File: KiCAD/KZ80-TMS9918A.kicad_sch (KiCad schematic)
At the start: 39 parts

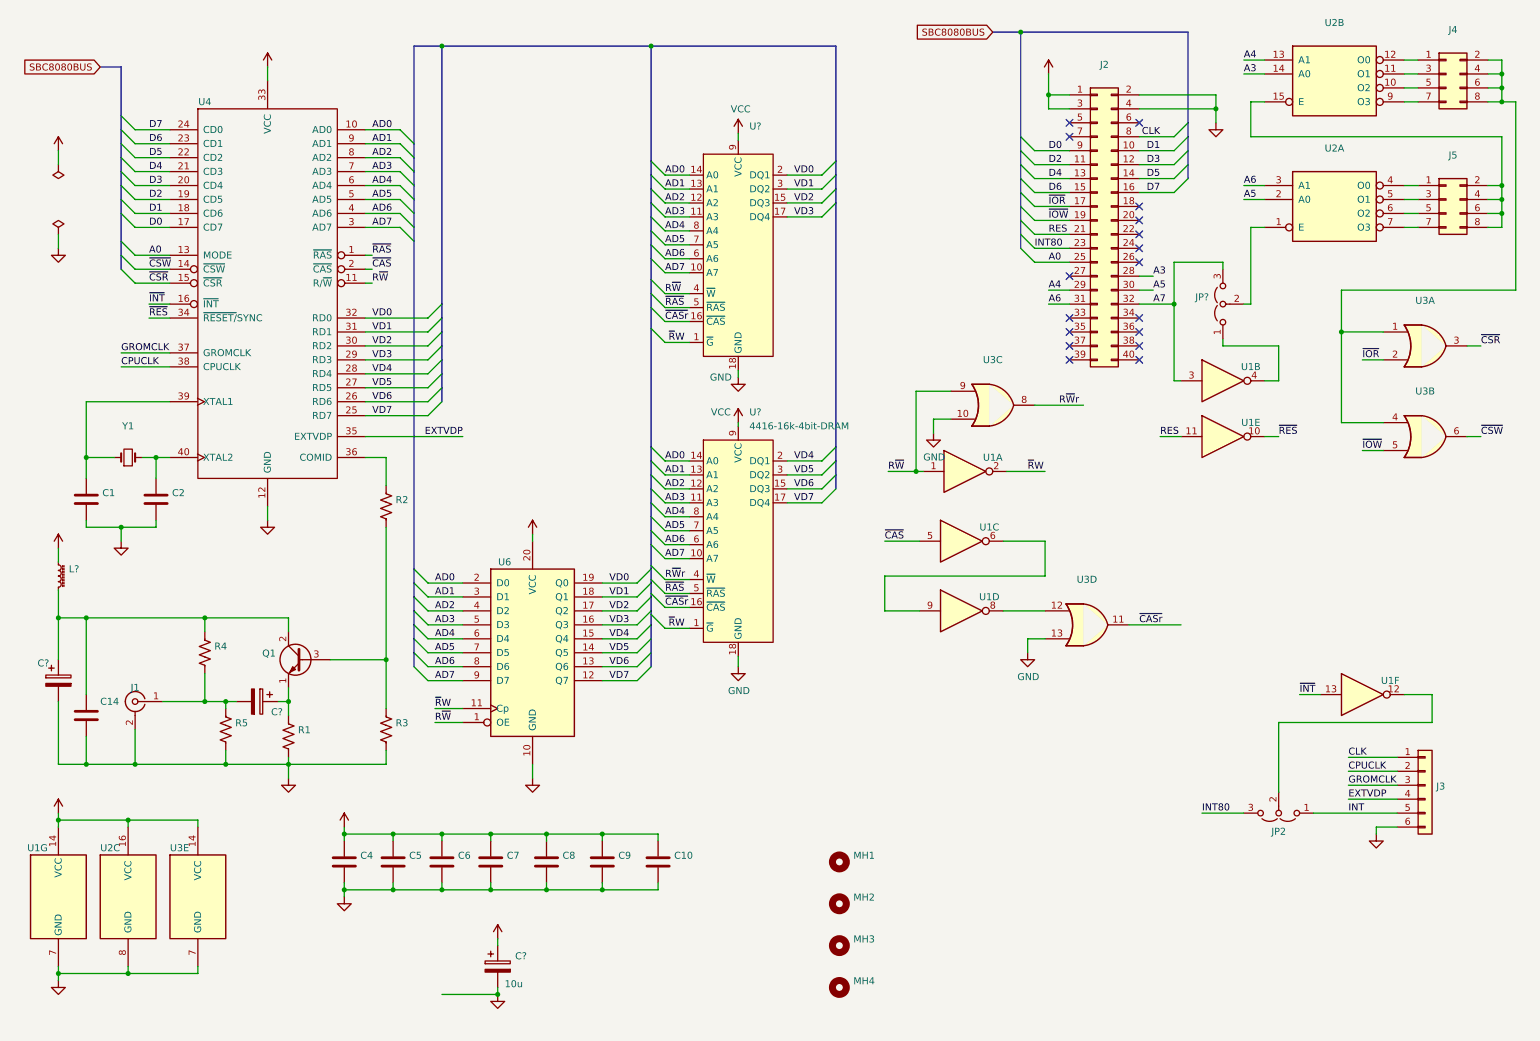
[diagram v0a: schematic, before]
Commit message: 4464 DRAM対応
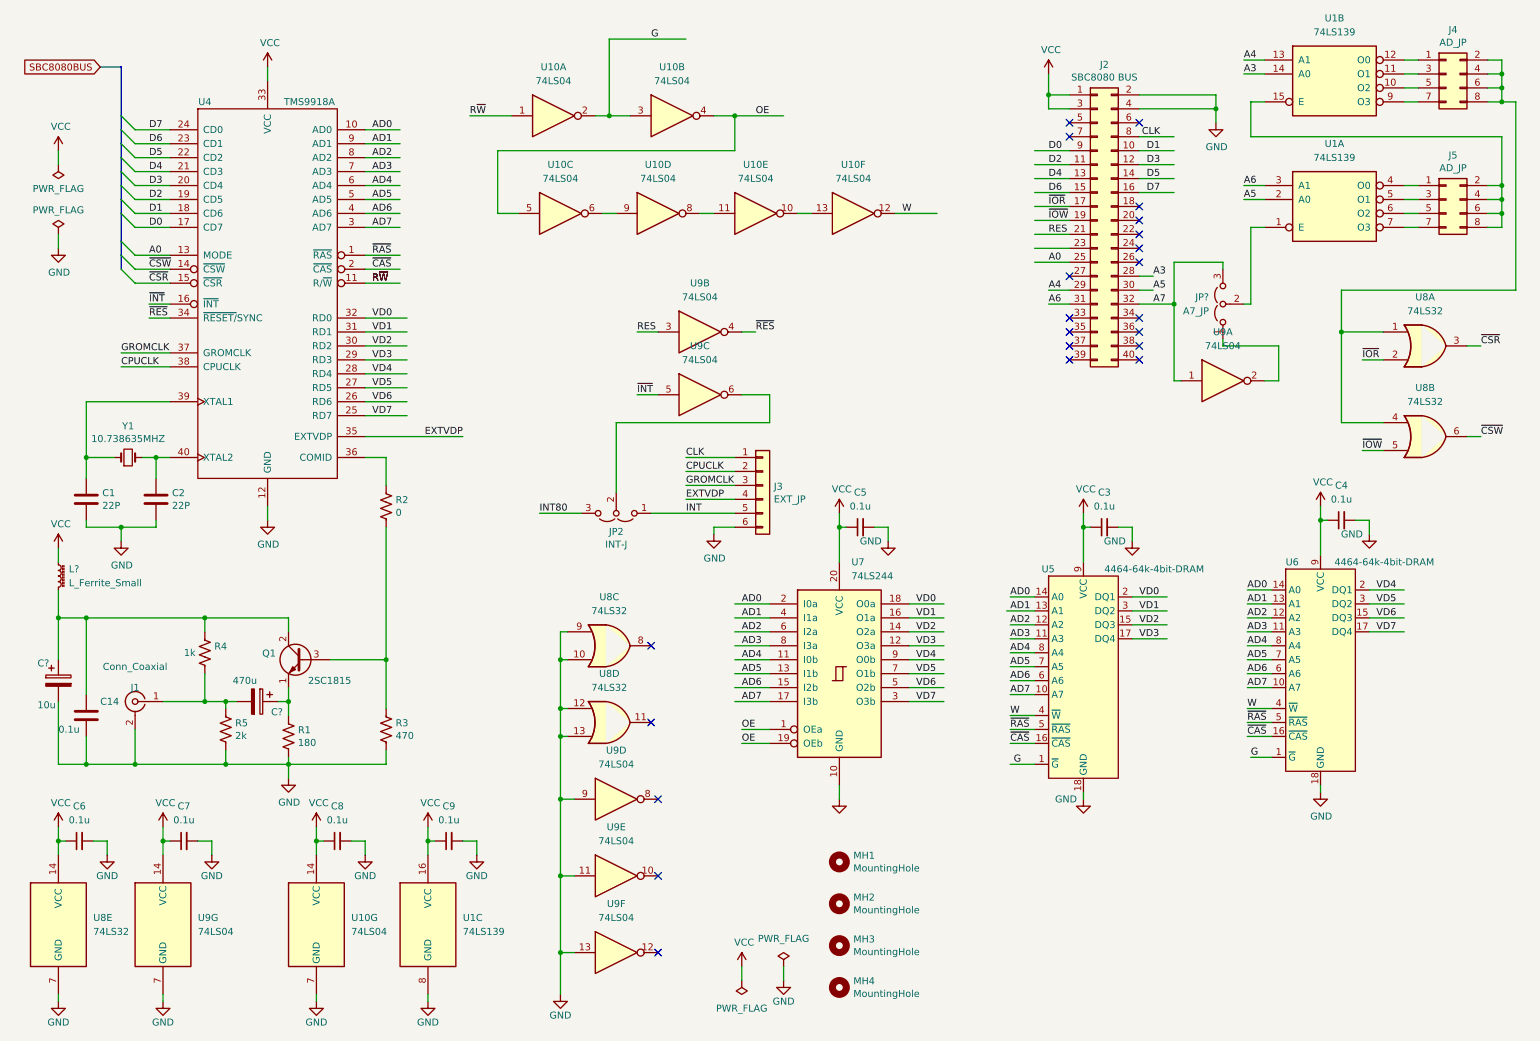
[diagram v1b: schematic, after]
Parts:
- removed C10, C4, C5, C6, C7, C8, C9: (no value), symbol Device:C
- removed C?: 10u, symbol Device:C_Polarized
- removed U1: (no value), symbol 74xx:74HCT04
- removed U2: (no value), symbol 74xx:74LS139
- removed U3: (no value), symbol 74xx:74LS32
- removed U6: (no value), symbol 74xx:74LS574
- removed U?: 4416-16k-4bit-DRAM, symbol DRAM:4416-16k-4bit-DRAM
- removed U?: (no value), symbol DRAM:4416-16k-4bit-DRAM
- added C3, C4, C5, C6, C7, C8, C9: 0.1u, symbol Device:C_Small
- added U1: 74LS139, symbol 74xx:74LS139
- added U10, U9: 74LS04, symbol 74xx:74LS04
- added U5, U6: 4464-64k-4bit-DRAM, symbol DRAM:4416-16k-4bit-DRAM
- added U7: 74LS244, symbol 74xx:74LS244
- added U8: 74LS32, symbol 74xx:74LS32
- C1, C2: value (none) -> 22P; footprint (none) -> Capacitor_THT:C_Disc_D3.0mm_W1.6mm_P2.50mm
- C14: value (none) -> 0.1u; footprint (none) -> Capacitor_THT:C_Disc_D3.0mm_W1.6mm_P2.50mm
- C?: value (none) -> 470u
- C?: value (none) -> 10u
- J1: value (none) -> Conn_Coaxial; footprint (none) -> RCACon:RCAConAE
- J2: value (none) -> SBC8080 BUS; footprint (none) -> Connector_PinHeader_2.54mm:PinHeader_2x20_P2.54mm_Horizontal
- J3: value (none) -> EXT_JP; footprint (none) -> Connector_PinHeader_2.54mm:PinHeader_1x06_P2.54mm_Horizontal
- J4, J5: value (none) -> AD_JP; footprint (none) -> Connector_PinHeader_2.54mm:PinHeader_2x04_P2.54mm_Vertical
- JP2: value (none) -> INT-J; footprint (none) -> Connector_PinHeader_2.54mm:PinHeader_1x03_P2.54mm_Vertical
- JP?: value (none) -> A7_JP
- L?: value (none) -> L_Ferrite_Small
- MH1, MH2, MH3, MH4: value (none) -> MountingHole; footprint (none) -> MountingHole:MountingHole_3.2mm_M3
- Q1: value (none) -> 2SC1815; footprint (none) -> Package_TO_SOT_THT:TO-92_Inline_Wide
- R1: value (none) -> 180; footprint (none) -> Resistor_THT:R_Axial_DIN0207_L6.3mm_D2.5mm_P10.16mm_Horizontal
- R2: value (none) -> 0; footprint (none) -> Resistor_THT:R_Axial_DIN0207_L6.3mm_D2.5mm_P10.16mm_Horizontal
- R3: value (none) -> 470; footprint (none) -> Resistor_THT:R_Axial_DIN0207_L6.3mm_D2.5mm_P10.16mm_Horizontal
- R4: value (none) -> 1k; footprint (none) -> Resistor_THT:R_Axial_DIN0207_L6.3mm_D2.5mm_P10.16mm_Horizontal
- R5: value (none) -> 2k; footprint (none) -> Resistor_THT:R_Axial_DIN0207_L6.3mm_D2.5mm_P10.16mm_Horizontal
- U4: value (none) -> TMS9918A; footprint (none) -> Package_DIP:DIP-40_W15.24mm_Socket
- Y1: value (none) -> 10.738635MHZ; footprint (none) -> Crystal:Crystal_HC49-U_Vertical
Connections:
- net A3: now also U1.14 (A0)
- net A4: now also U1.13 (A1)
- net A5: now also U1.2 (A0)
- net A6: now also U1.3 (A1)
- net A7: now also U9.1
- net AD0: now also U5.14 (A0), U6.14 (A0), U7.2 (I0a)
- net AD1: now also U5.13 (A1), U6.13 (A1), U7.4 (I1a)
- net AD2: now also U5.12 (A2), U6.12 (A2), U7.6 (I2a)
- net AD3: now also U5.11 (A3), U6.11 (A3), U7.8 (I3a)
- net AD4: now also U5.8 (A4), U6.8 (A4), U7.11 (I0b)
- net AD5: now also U5.7 (A5), U6.7 (A5), U7.13 (I1b)
- net AD6: now also U5.6 (A6), U6.6 (A6), U7.15 (I2b)
- net AD7: now also U5.10 (A7), U6.10 (A7), U7.17 (I3b)
- net GND: now also C3.2, C4.2, C5.2, C6.2, C7.2, C8.2, C9.2, U1.8 (GND), U10.7 (GND), U5.18 (GND), U6.18 (GND), U7.10 (GND), U8.10, U8.12, U8.13, U8.7 (GND), U8.9, U9.11, U9.13, U9.7 (GND), U9.9
- net INT80: no longer J2.23 (Pin_23)
- net RES: now also U9.3
- net R~{W}: now also U10.1
- net VCC: now also C3.1, C4.1, C5.1, C6.1, C7.1, C8.1, C9.1, U1.16 (VCC), U10.14 (VCC), U5.9 (VCC), U6.9 (VCC), U7.20 (VCC), U8.14 (VCC), U9.14 (VCC)
- net VD0: now also U5.2 (DQ1), U7.18 (O0a)
- net VD1: now also U5.3 (DQ2), U7.16 (O1a)
- net VD2: now also U5.15 (DQ3), U7.14 (O2a)
- net VD3: now also U5.17 (DQ4), U7.12 (O3a)
- net VD4: now also U6.2 (DQ1), U7.9 (O0b)
- net VD5: now also U6.3 (DQ2), U7.7 (O1b)
- net VD6: now also U6.15 (DQ3), U7.5 (O2b)
- net VD7: now also U6.17 (DQ4), U7.3 (O3b)
- net ~{CAS}: now also U5.16 (~{CAS}), U6.16 (~{CAS})
- net ~{CSR}: now also U8.3
- net ~{CSW}: now also U8.6
- net ~{INT}: now also U9.5
- net ~{IOR}: now also U8.2
- net ~{IOW}: now also U8.5
- net ~{RAS}: now also U5.5 (~{RAS}), U6.5 (~{RAS})
- net ~{RES}: now also U9.4
- net at JP?.1 (A): now also U9.2
- net at J4.5 (Pin_5): now also U1.10 (O2)
- net at J4.3 (Pin_3): now also U1.11 (O1)
- net at J4.1 (Pin_1): now also U1.12 (O0)
- net at J5.2 (Pin_2), J5.4 (Pin_4), J5.6 (Pin_6)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: now also U1.15 (E)
- net at J4.7 (Pin_7): now also U1.9 (O3)
- net at JP?.2 (C): now also U1.1 (E)
- net at J5.1 (Pin_1): now also U1.4 (O0)
- net at J5.3 (Pin_3): now also U1.5 (O1)
- net at J5.5 (Pin_5): now also U1.6 (O2)
- net at J5.7 (Pin_7): now also U1.7 (O3)
- net at JP2.2 (C): now also U9.6
- net at J4.2 (Pin_2), J4.4 (Pin_4), J4.6 (Pin_6)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: now also U8.1, U8.4
- new net: U10.10, U10.13
- new net: U10.11, U10.8
- new net: U10.6, U10.9
- new net G: U10.2, U10.3, U5.1 (~{G}), U6.1 (~{G})
- new net OE: U10.4, U10.5, U7.1 (OEa), U7.19 (OEb)
- new net W: U10.12, U5.4 (~{W}), U6.4 (~{W})
- no-connect marks 17 -> 22
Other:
- moved on the sheet: J3, JP2

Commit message: パスコン追加等
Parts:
- added C12: 10u, symbol Device:C_Polarized_Small
- added C8: 0.1u, symbol Device:C_Small
- U1: renamed from U8; value 74LS32 -> 74HCT32
- U2, U4: renamed from U9; value 74LS04 -> 74HCT04
- U2, U4: renamed from U10; value 74LS04 -> 74HCT04
- U5: renamed from U1; value 74LS139 -> 74HCT139
- U6: renamed from U7; value 74LS244 -> 74HCT244
- gave numbers to parts that had none: 4
- renumbered C9 to C10, C5 to C11, C3 to C13, C4 to C14, C6 to C2, C1 to C3, C14 to C4, C2 to C5, C7 to C6, C8 to C9, J3 to J2, J2 to J3, JP2 to JP1, R4 to R1, R5 to R2, R1 to R3, R2 to R4, R3 to R5, U4 to U3, U5 to U7, U6 to U8
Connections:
- net GND: now also C12.2, C8.2
- net INT80: now also J3.23 (Pin_23)
- net VCC: now also C12.1, C8.1
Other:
- moved on the sheet: J2, JP1, MH1, MH2, MH3, MH4, U4B, U4C

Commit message: 64k DRAM版 ガーバー出力
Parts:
- C1, C12, C7: footprint (none) -> Capacitor_THT:CP_Radial_D5.0mm_P2.50mm
- C10, C11, C13, C14, C2, C6, C8, C9: footprint (none) -> Capacitor_THT:C_Disc_D3.0mm_W1.6mm_P2.50mm
- JP2: footprint (none) -> Connector_PinHeader_2.54mm:PinHeader_1x03_P2.54mm_Vertical
- L1: footprint (none) -> Resistor_THT:R_Axial_DIN0207_L6.3mm_D2.5mm_P10.16mm_Horizontal
- U1, U2, U4: footprint (none) -> Package_DIP:DIP-14_W7.62mm_Socket
- U2: renamed from U4; footprint (none) -> Package_DIP:DIP-14_W7.62mm_Socket
- U4: renamed from U2; footprint (none) -> Package_DIP:DIP-14_W7.62mm_Socket
- U5: footprint (none) -> Package_DIP:DIP-16_W7.62mm_Socket
- U6: footprint (none) -> Package_DIP:DIP-20_W7.62mm_Socket
- U7, U8: footprint (none) -> Package_DIP:DIP-18_W7.62mm_Socket
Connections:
- net AD0: no longer U7.14 (A0), U8.14 (A0)
- net AD1: now also U7.6 (A6), U8.6 (A6); no longer U7.13 (A1), U8.13 (A1)
- net AD2: now also U7.7 (A5), U8.7 (A5); no longer U7.12 (A2), U8.12 (A2)
- net AD3: now also U7.8 (A4), U8.8 (A4); no longer U7.11 (A3), U8.11 (A3)
- net AD4: now also U7.11 (A3), U8.11 (A3); no longer U7.8 (A4), U8.8 (A4)
- net AD5: now also U7.12 (A2), U8.12 (A2); no longer U7.7 (A5), U8.7 (A5)
- net AD6: now also U7.13 (A1), U8.13 (A1); no longer U7.6 (A6), U8.6 (A6)
- net AD7: now also U7.14 (A0), U8.14 (A0); no longer U7.10 (A7), U8.10 (A7)
- net GND: now also U7.10 (A7), U8.10 (A7)
